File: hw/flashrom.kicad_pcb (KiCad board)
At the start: 2 copper layers, 19 x 52.1 mm, 14 parts, among them J1 Conn_01x04_Pin, J2 Conn_01x03_Pin, J3 BG306-04-A-1-0400-L, U1 29F800-TSOP, U2 Kickstart_Socket_A4000

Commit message: set gerber and drill output options
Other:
- rule pad_to_mask_clearance: 0.05 -> 0
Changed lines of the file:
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@@
       (dielectric_constraints no)
     )
-    (pad_to_mask_clearance 0.05)
-    (solder_mask_min_width 0.15)
+    (pad_to_mask_clearance 0)
     (allow_soldermask_bridges_in_footprints yes)
     (pcbplotparams
@@
       (plot_on_all_layers_selection 0x0000000_00000000)
       (disableapertmacros false)
-      (usegerberextensions false)
+      (usegerberextensions true)
       (usegerberattributes false)
       (usegerberadvancedattributes false)
@@
       (psa4output false)
       (plotreference true)
-      (plotvalue true)
+      (plotvalue false)
       (plotinvisibletext false)
       (sketchpadsonfab false)
-      (subtractmaskfromsilk false)
+      (subtractmaskfromsilk true)
       (outputformat 1)
       (mirror false)
-      (drillshape 1)
+      (drillshape 0)
       (scaleselection 1)
-      (outputdirectory "")
+      (outputdirectory "output/")
     )
   )

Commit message: change product text to github repo url
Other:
- board text added: "github.com/ matthiesenj/ flashrom V0.9"
- board text removed: "27C800 Flashrom"
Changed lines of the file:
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@@
     (pad_to_mask_clearance 0)
     (allow_soldermask_bridges_in_footprints yes)
+    (aux_axis_origin 50.8 50.8)
     (pcbplotparams
       (layerselection 0x00010fc_ffffffff)
@@
     (effects (font (size 1.7 1.5) (thickness 0.18)) (justify left bottom))
   )
-  (gr_text "27C800\nFlashrom" (at 58.42 71.755) (layer "F.SilkS")
-    (effects (font (size 2 1.8) (thickness 0.3)) (justify bottom))
+  (gr_text "github.com/\nmatthiesenj/\nflashrom\n\nV0.9" (at 53.34 72.39) (layer "F.SilkS")
+    (effects (font (size 1 1) (thickness 0.15)) (justify left bottom))
   )
   (segment (start 58.661 97.282) (end 58.674 97.295) (width 0.25) (layer "F.Cu") (net 1))

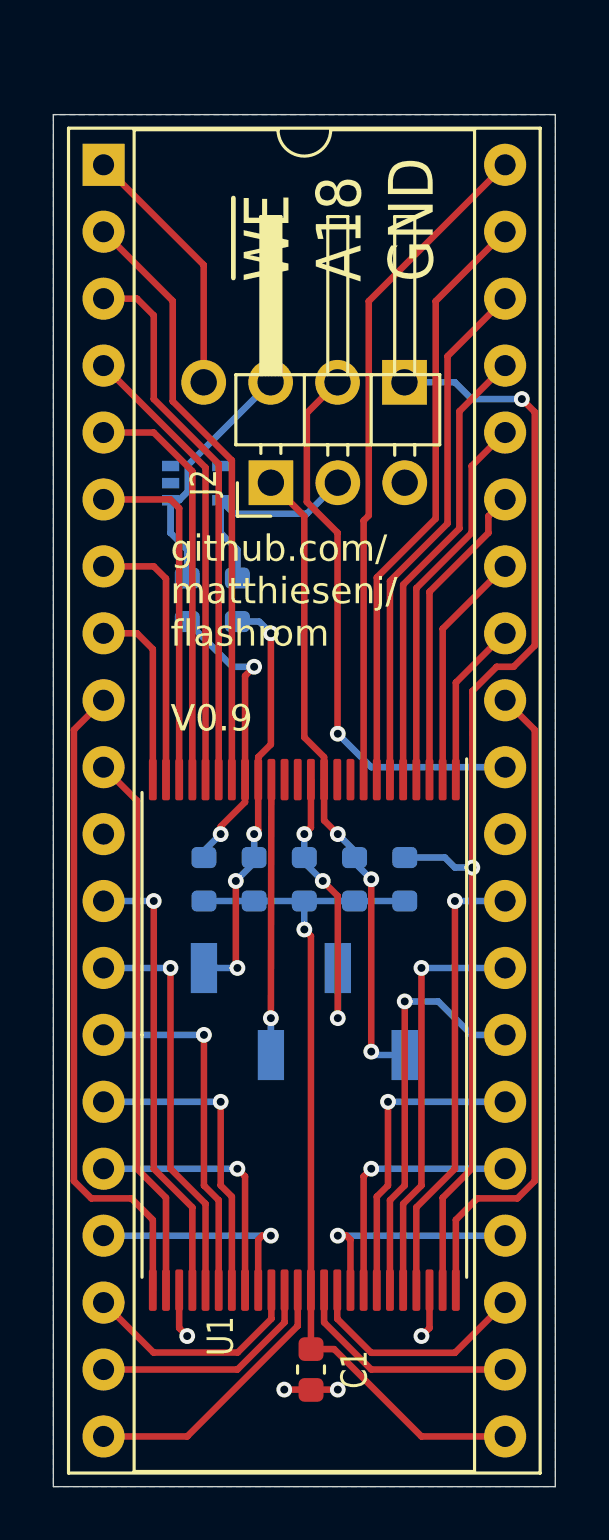
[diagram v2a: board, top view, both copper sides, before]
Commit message: narrow pcb to 18.3mm width to fit a4000d
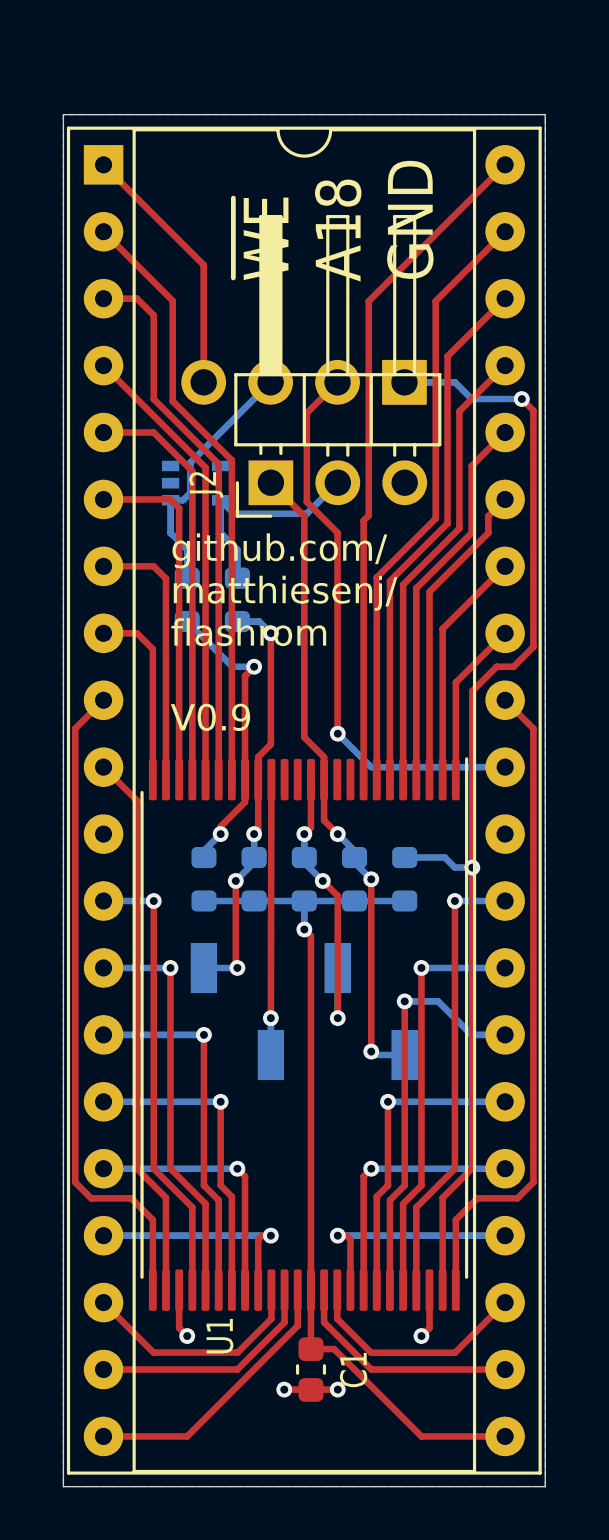
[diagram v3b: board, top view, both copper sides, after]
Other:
- board size 19 x 52.1 mm -> 18.3 x 52.1 mm
- board text added: "Must be < ~18.5 mm wide to fit side by side in A4000D"

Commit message: switch j3 footprint to horizontal pin header
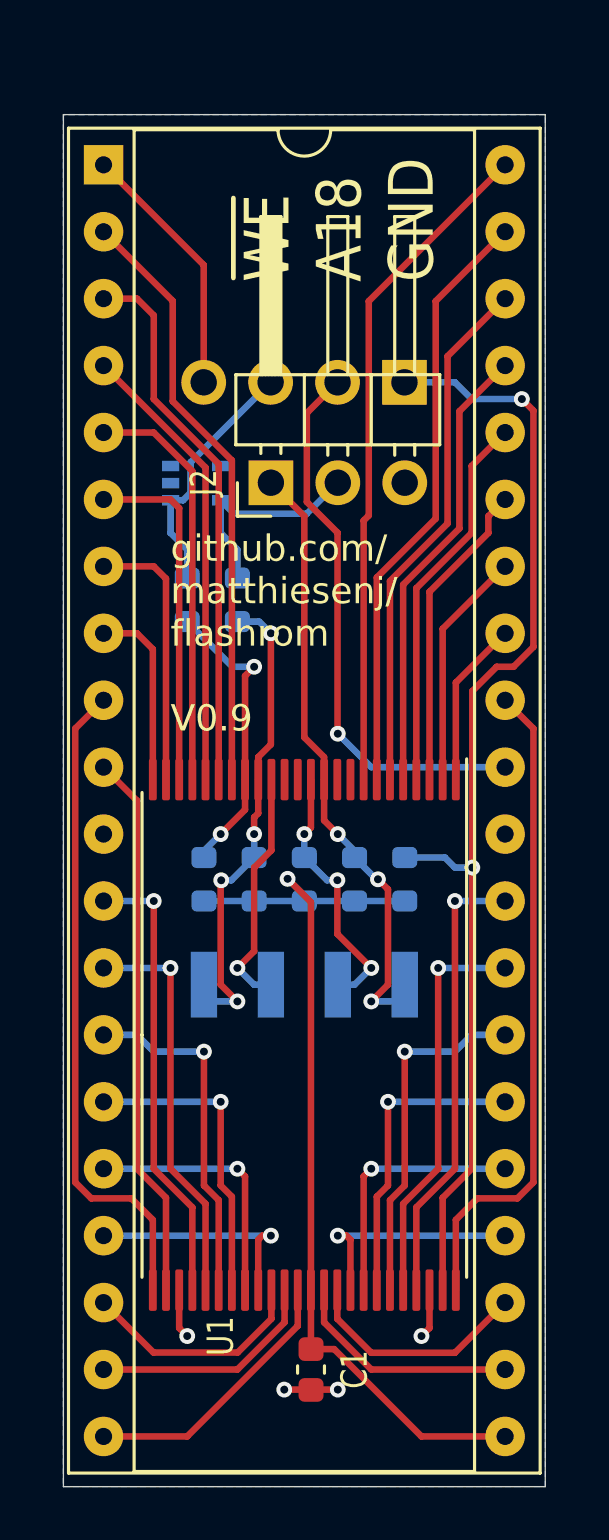
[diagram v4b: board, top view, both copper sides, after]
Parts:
- J3: value BG306-04-A-1-0400-L -> Conn_01x04_Pin; footprint Connector_PinSocket_2.54mm:PinSocket_1x04_P2.54mm_Vertical_SMD_Pin1Left -> Connector_Harwin:Harwin_M20-89004xx_1x04_P2.54mm_Horizontal
- moved J3 4.50 mm to (58.4, 87.4), turned to -90 degrees
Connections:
- J3 pad 1: /~{WE} -> /A18
- J3 pad 2: /~{RESET} -> /RY/~{BY}
- J3 pad 3: /RY/~{BY} -> /~{RESET}
- J3 pad 4: /A18 -> /~{WE}
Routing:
- net /A18: track 16.0 -> 18.6 mm
- net +5V: track 33.5 -> 35.7 mm
- net /D14: track 15.5 -> 13.4 mm
- net /~{RESET}: track 11.3 -> 9.81 mm
- net /RY/~{BY}: track 10.5 -> 9.21 mm
- net /~{WE}: track 24.5 -> 23.7 mm

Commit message: switch j1 and j2 footprints to smd horizontal header
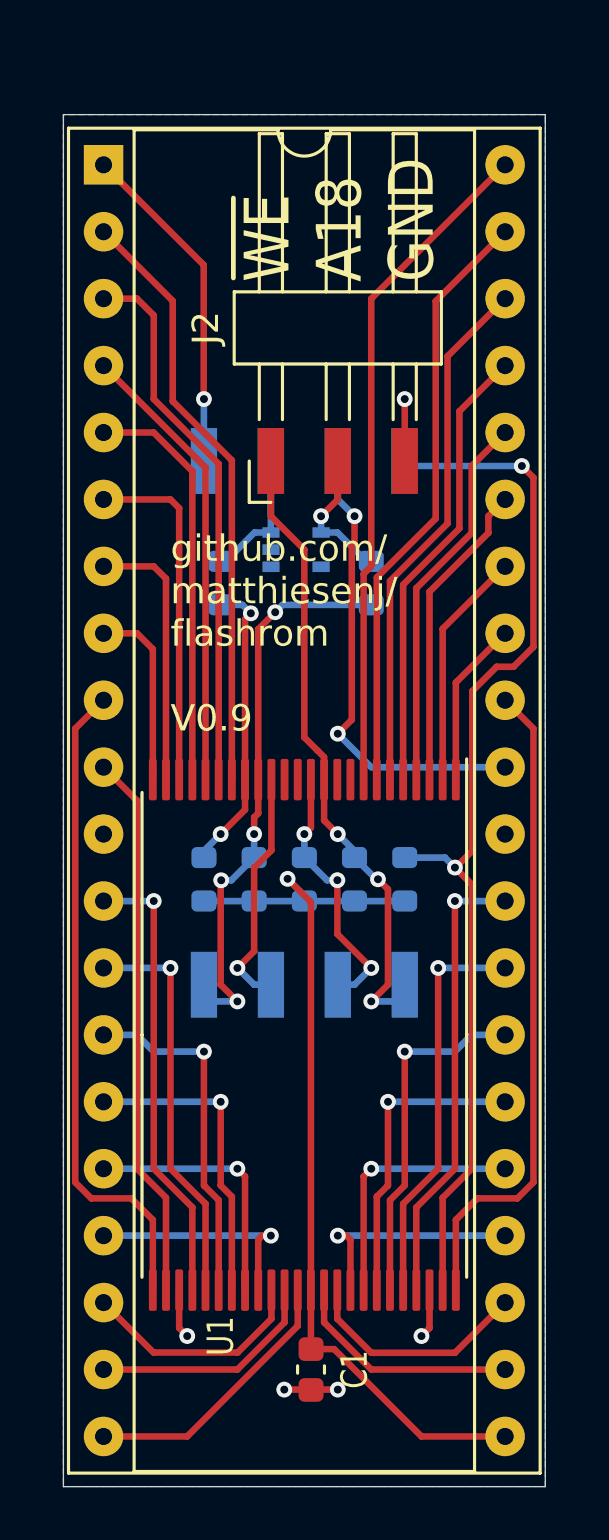
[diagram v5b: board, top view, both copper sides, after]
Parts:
- J1: footprint Connector_PinHeader_2.54mm:PinHeader_1x04_P2.54mm_Horizontal -> Connector_Harwin:Harwin_M20-89004xx_1x04_P2.54mm_Horizontal
- J2: footprint Connector_PinHeader_2.54mm:PinHeader_1x03_P2.54mm_Horizontal -> Connector_Harwin:Harwin_M20-89003xx_1x03_P2.54mm_Horizontal
- moved J2 6.84 mm to (59.7, 56.5)
- moved R2 5.12 mm to (61.0, 66.7)
- moved D1 4.57 mm to (58.1, 65.4)
- moved J1 4.57 mm to (58.4, 56.5)
- moved R1 1.42 mm to (55.2, 66.7)
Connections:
- D1 pad 1: /TVS1 -> unconnected-(D1-K-Pad1)
- D1 pad 3: unconnected-(D1-K-Pad3) -> /TVS1
- D1 pad 4: unconnected-(D1-K-Pad4) -> /TVS3
- D1 pad 5: /TVS3 -> unconnected-(D1-K-Pad5)
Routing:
- net /TVS1: track 9.54 -> 5.08 mm
- net /OA17: track 21.2 -> 17.8 mm, vias 1 -> 2
- net /A18: track 18.6 -> 21.8 mm
- net /TVS3: track 8.36 -> 5.34 mm, vias 0 -> 1
- net /NA17: track 9.83 -> 12.8 mm, vias 0 -> 1
- net /~{BYTE}: track 43.2 -> 40.4 mm
- net GND: track 5.78 -> 8.13 mm, vias 4 -> 5
- net /~{WE}: track 23.7 -> 24.6 mm
